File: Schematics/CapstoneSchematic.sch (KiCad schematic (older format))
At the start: 20 parts, among them J1 ArduinoRGBShield, J2 VoltageIn, T1 Temp Sensor, U6 LaserSensor, U7 CMP12-CapstoneLib

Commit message: Added Michael's alarm pcb rev
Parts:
- removed 2A1: Fuse, symbol Device:Fuse
- removed SAS1: SnapActionSwitch, TerminalBlock_MetzConnect:TerminalBlock_MetzConnect_Type094_RT03502HBLU_1x02_P5.00mm_Horizontal, symbol CapstoneSchematic:SnapActionSwitch
- added C?: C, symbol Device:C
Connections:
- net +5V: no longer SAS2.1 (COM_T1)
- net GND: now also SAS2.1 (COM_T1)
- net LED_G: no longer A1.22 (D7)
- net LED_R: no longer A1.21 (D6)
- net LoRa3: no longer A1.16 (D1/TX)
- net LoRa4: no longer A1.15 (D0/RX)
- net at RM1.6 (COMM): now also LA1.1 (VNeg), C?.1; no longer SAS2.2 (COM_T2)
- net at RM1.9 (COMM): now also LA1.2 (Vpos), C?.2
- net SAS_Int1: no longer names the net of A1.17 (D2)

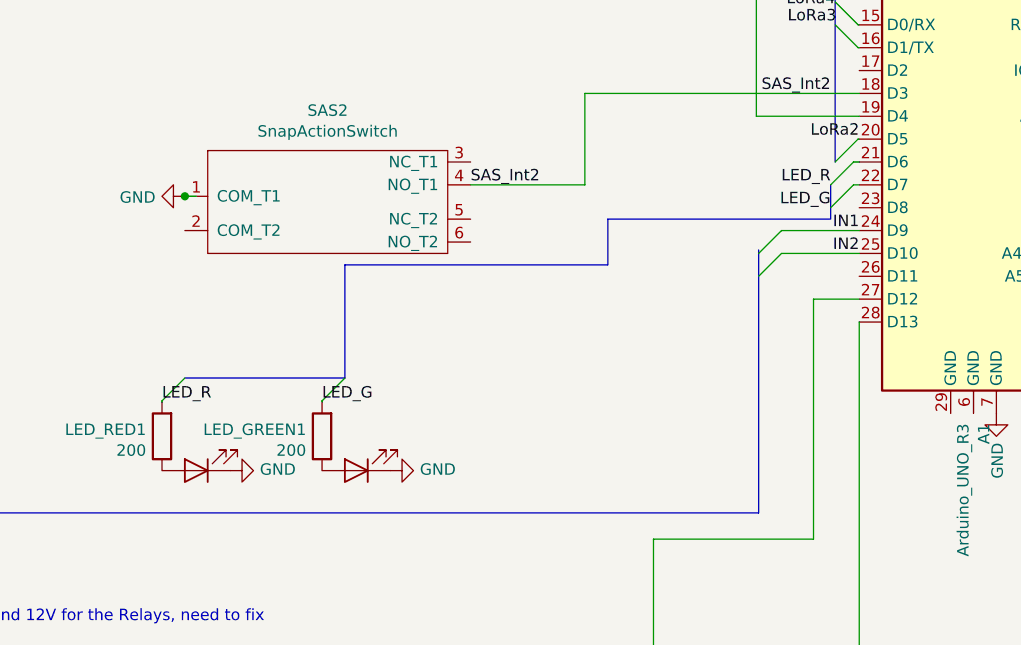
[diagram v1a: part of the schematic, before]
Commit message: Changed the leds
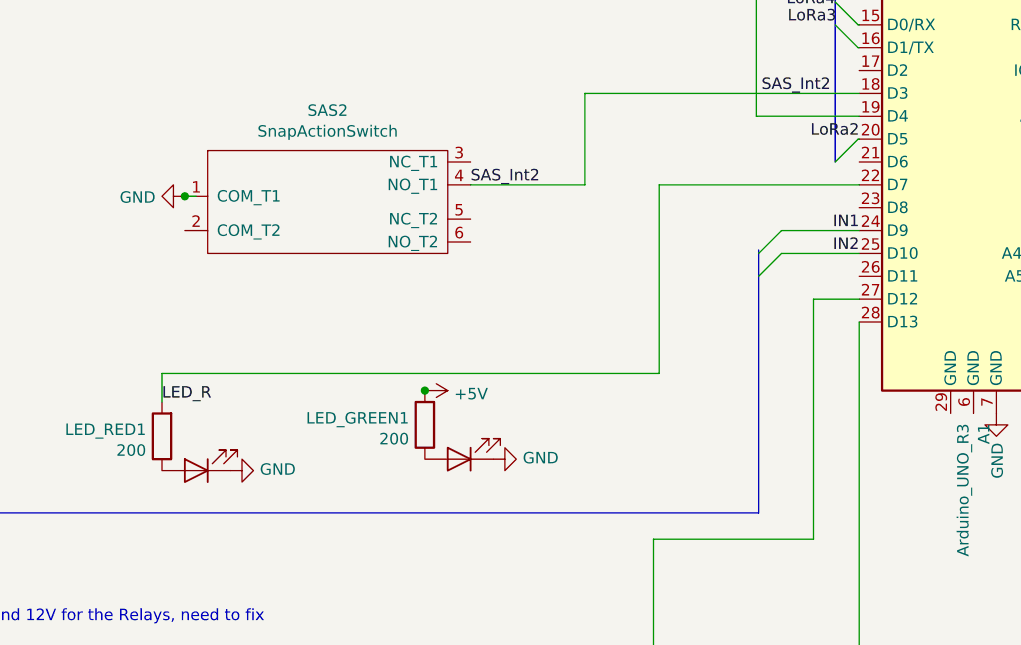
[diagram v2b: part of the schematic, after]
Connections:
- net labels removed: LED_G
- wire segments 63 -> 64
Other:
- moved on the sheet: LED_GREEN1
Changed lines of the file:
@@
 L CapstoneSchematic:LEDModule LED_GREEN1
 U 1 1 5DC91461
-P 4300 4400
-F 0 "LED_GREEN1" H 4231 4279 50  0000 R CNN
-F 1 "200" H 4231 4188 50  0000 R CNN
-F 2 "TerminalBlock_MetzConnect:TerminalBlock_MetzConnect_Type094_RT03502HBLU_1x02_P5.00mm_Horizontal" V 4370 4250 50  0001 C CNN
-F 3 "~" H 4300 4250 50  0001 C CNN
-	1    4300 4400
+P 4750 4350
+F 0 "LED_GREEN1" H 4681 4229 50  0000 R CNN
+F 1 "200" H 4681 4138 50  0000 R CNN
+F 2 "TerminalBlock_MetzConnect:TerminalBlock_MetzConnect_Type094_RT03502HBLU_1x02_P5.00mm_Horizontal" V 4820 4200 50  0001 C CNN
+F 3 "~" H 4750 4200 50  0001 C CNN
+	1    4750 4350
 	1    0    0    -1
 $EndComp
@@
 L power:GND #PWR0116
 U 1 1 5DCB250A
-P 4600 4700
-F 0 "#PWR0116" H 4600 4450 50  0001 C CNN
-F 1 "GND" V 4605 4572 50  0000 R CNN
-F 2 "" H 4600 4700 50  0001 C CNN
-F 3 "" H 4600 4700 50  0001 C CNN
-	1    4600 4700
+P 5050 4650
+F 0 "#PWR0116" H 5050 4400 50  0001 C CNN
+F 1 "GND" V 5055 4522 50  0000 R CNN
+F 2 "" H 5050 4650 50  0001 C CNN
+F 3 "" H 5050 4650 50  0001 C CNN
+	1    5050 4650
 	0    -1   -1   0
 $EndComp
@@
 	6200 3150 6650 3150
 Entry Wire Line
-	6645 3250 6545 3350
-Entry Wire Line
-	6625 3350 6525 3450
-Entry Wire Line
-	6625 3450 6525 3550
-Wire Bus Line
-	4400 3800 5550 3800
-Wire Bus Line
-	5550 3800 5550 3600
-Entry Wire Line
 	6210 3750 6310 3650
 Entry Wire Line
@@
 	6310 3750 6650 3750
 Wire Wire Line
-	6625 3450 6650 3450
-Wire Wire Line
-	6625 3350 6650 3350
-Wire Bus Line
-	6520 3600 5550 3600
-Wire Wire Line
 	6645 3250 6650 3250
 Wire Wire Line
@@
 Wire Bus Line
 	695  4885 6210 4885
-Text Label 4300 4400 0    50   ~ 0
-LED_G
-Wire Bus Line
-	3700 4295 4400 4295
-Entry Wire Line
-	3600 4395 3700 4295
-Wire Wire Line
-	4300 4395 4300 4400
-Wire Wire Line
-	3600 4395 3600 4400
-Text Label 3600 4400 0    50   ~ 0
-LED_R
-Wire Bus Line
-	4400 3800 4400 4295
-Entry Wire Line
-	4400 4295 4300 4395
+Wire Wire Line
+	4750 4345 4750 4350
 Text Label 6650 3750 2    50   ~ 0
 IN2
@@
 Text Label 6650 3250 2    50   ~ 0
 LoRa2
-Text Label 6525 3450 2    50   ~ 0
-LED_R
-Text Label 6525 3550 2    50   ~ 0
-LED_G
 Wire Bus Line
 	6545 2500 6550 2500
@@
 Text Label 6525 3050 2    50   ~ 0
 SAS_Int2
+Text Label 3600 4400 0    50   ~ 0
+LED_R
+$Comp
+L power:+5V #PWR?
+U 1 1 5E8A92AF
+P 4750 4350
+F 0 "#PWR?" H 4750 4200 50  0001 C CNN
+F 1 "+5V" V 4765 4478 50  0000 L CNN
+F 2 "" H 4750 4350 50  0001 C CNN
+F 3 "" H 4750 4350 50  0001 C CNN
+	1    4750 4350
+	0    1    1    0
+$EndComp
+Connection ~ 4750 4350
+Wire Wire Line
+	3600 4275 3600 4400
+Entry Wire Line
+	6645 3250 6545 3350
+Wire Wire Line
+	5775 3450 6650 3450
 Wire Bus Line
 	695  4050 695  4885
 Wire Bus Line
-	6525 3450 6525 3600
+	6210 3735 6210 4885
+Wire Bus Line
+	6545 2500 6545 3350
 Wire Bus Line
 	4250 1500 4250 1700
-Wire Bus Line
-	6545 2500 6545 3350
-Wire Bus Line
-	6210 3735 6210 4885
+Wire Wire Line
+	5775 4275 3600 4275
+Wire Wire Line
+	5775 3450 5775 4275
 $EndSCHEMATC

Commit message: Fixed most of schematic, need to update linear regulator footprint
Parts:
- removed C?: C, symbol Device:C
- added SAS1: SnapActionSwitch, TerminalBlock_MetzConnect:TerminalBlock_MetzConnect_Type094_RT03503HBLU_1x03_P5.00mm_Horizontal, symbol CapstoneSchematic:SnapActionSwitch
- renumbered J2 to J1, J1 to J2, U6 to U1, U7 to U2
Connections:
- net labels added: SAS_Int1
- wire segments 64 -> 70
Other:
- moved on the sheet: SAS2
